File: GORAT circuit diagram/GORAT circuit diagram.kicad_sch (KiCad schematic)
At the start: 41 parts, among them J1 NMJ4HFD2, J2 NMJ4HFD2, J3 Barrel_Jack_PTH_Slot, U1 LM308N

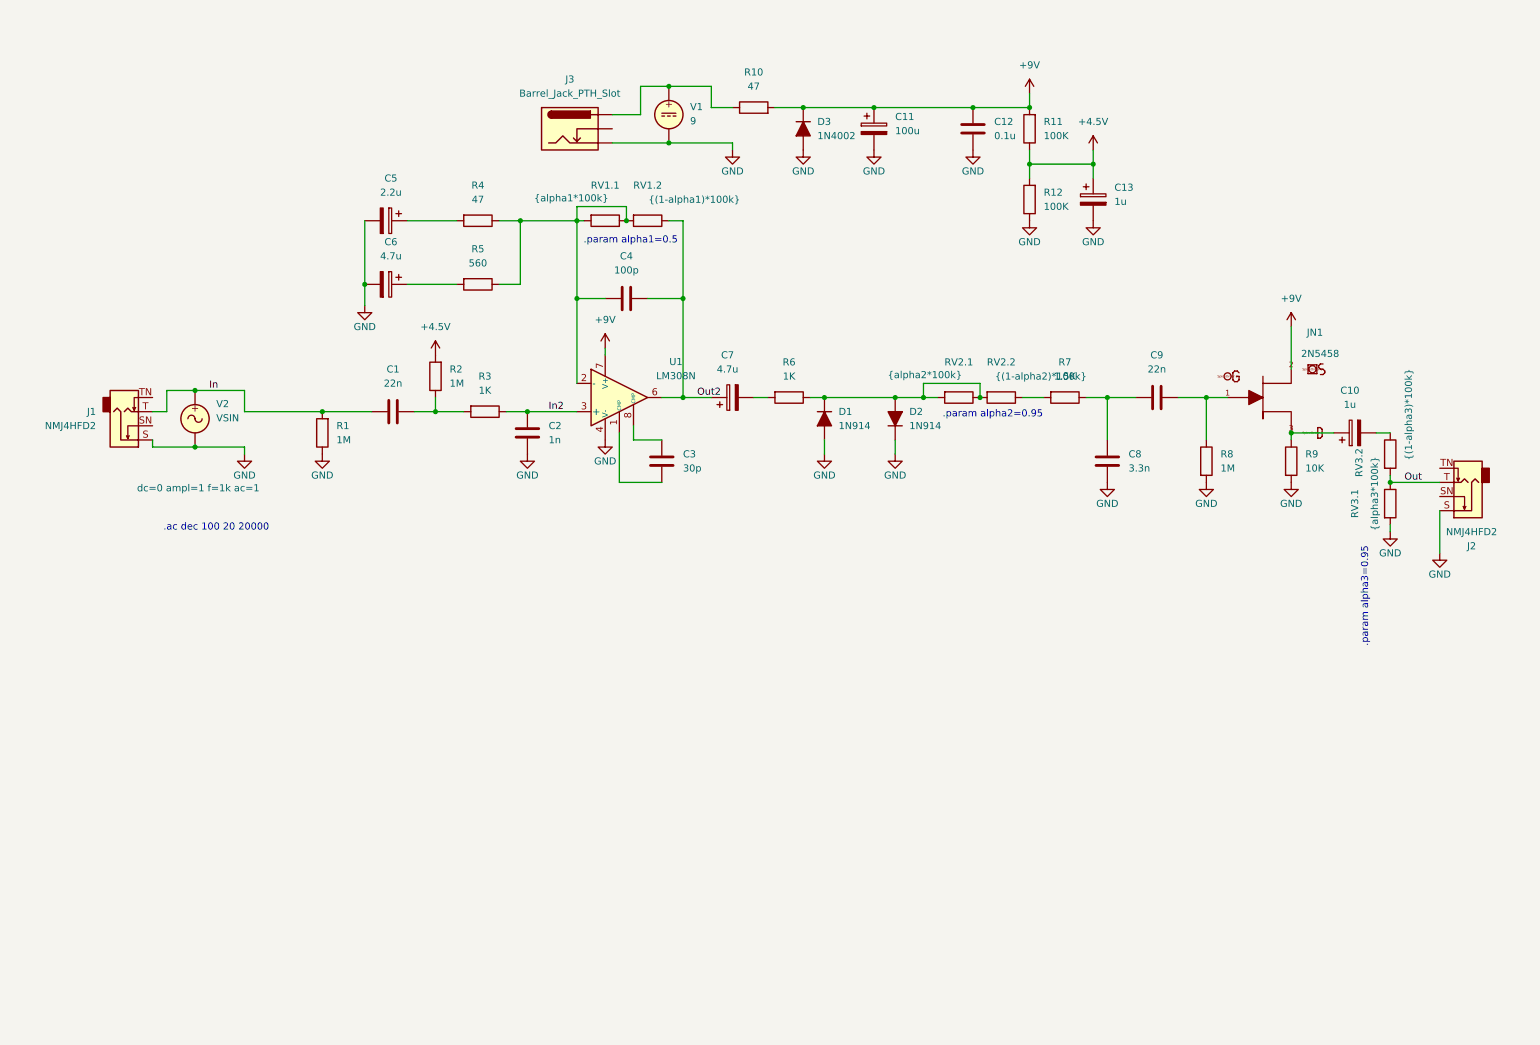
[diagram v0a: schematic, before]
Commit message: Update KiCad PCB and add backups
Replace GORAT circuit diagram.kicad_pcb with the full PCB data (expanded footprints, nets, layers and layout). Update related project files (GORAT circuit diagram.kicad_pro, .kicad_sch and fp-info-cache). Add multiple timestamped backup ZIPs under GORAT circuit diagram/GORAT circuit diagram-backups (dates 2026-02-27 and 2026-03-02).
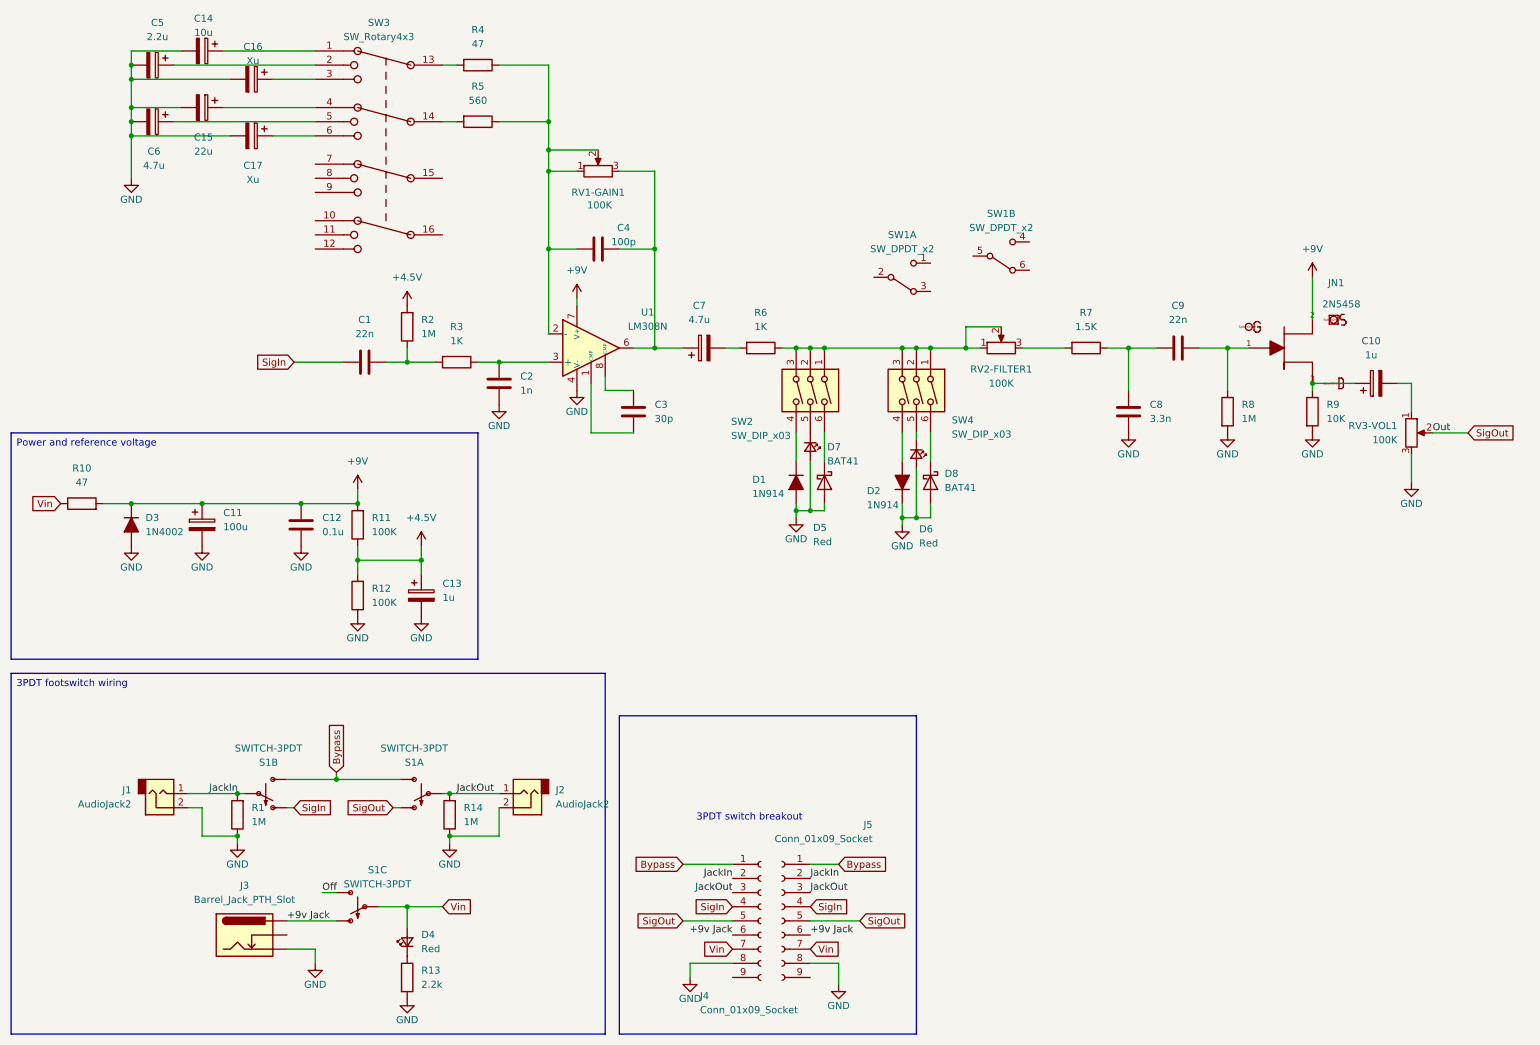
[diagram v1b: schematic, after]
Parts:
- removed J1, J2: NMJ4HFD2, Connector_Audio:Jack_6.35mm_Neutrik_NMJ4HFD2_Horizontal, symbol Connector_Audio:NMJ4HFD2
- removed RV1.1: {alpha1*100k}, symbol Device:R
- removed RV1.2: {(1-alpha1)*100k}, symbol Device:R
- removed RV2.1: {alpha2*100k}, symbol Device:R
- removed RV2.2: {(1-alpha2)*100k}, symbol Device:R
- removed RV3.1: {alpha3*100k}, symbol Device:R
- removed RV3.2: {(1-alpha3)*100k}, symbol Device:R
- removed V1: 9, symbol Simulation_SPICE:VDC
- removed V2: VSIN, symbol Simulation_SPICE:VSIN
- added C14: 10u, Capacitor_THT:CP_Radial_D5.0mm_P2.50mm, symbol Device:C_Polarized
- added C15: 22u, Capacitor_THT:CP_Radial_D5.0mm_P2.50mm, symbol Device:C_Polarized
- added C16, C17: Xu, Capacitor_THT:CP_Radial_D5.0mm_P2.50mm, symbol Device:C_Polarized
- added D4, D5, D6: Red, PCM_SparkFun-LED:LED_5mm_PTH_Red_NoSilk, symbol PCM_SparkFun-LED:LED_Red_5mm_PTH_NoSilk
- added D7, D8: BAT41, Diode_THT:D_DO-35_SOD27_P7.62mm_Horizontal, symbol Diode:BAT41
- added J1, J2: AudioJack2, Connector_Wire:SolderWire-0.75sqmm_1x02_P7mm_D1.25mm_OD3.5mm, symbol Connector_Audio:AudioJack2
- added J4, J5: Conn_01x09_Socket, Connector_PinHeader_2.54mm:PinHeader_1x09_P2.54mm_Vertical, symbol Connector:Conn_01x09_Socket
- added R13: 2.2k, Resistor_THT:R_Axial_DIN0207_L6.3mm_D2.5mm_P10.16mm_Horizontal, symbol Device:R
- added R14: 1M, Resistor_THT:R_Axial_DIN0207_L6.3mm_D2.5mm_P10.16mm_Horizontal, symbol Device:R
- added RV1-GAIN1, RV2-FILTER1, RV3-VOL1: 100K, Connector_Wire:SolderWire-0.75sqmm_1x03_P7mm_D1.25mm_OD3.5mm, symbol Device:R_Potentiometer
- added S1: SWITCH-3PDT, Daves customs:3PDT, symbol SparkFun-Electromechanical:SWITCH-3PDT
- added SW1: SW_DPDT_x2, symbol KRS_Switch:SW_DPDT_x2
- added SW2, SW4: SW_DIP_x03, symbol Switch:SW_DIP_x03
- added SW3: SW_Rotary4x3, Daves customs:Rotary Switch, symbol KRS_Switch:SW_Rotary4x3
- C1, C12, C2, C3, C4, C8, C9: footprint (none) -> Capacitor_THT:C_Disc_D4.7mm_W2.5mm_P5.00mm
- C10, C11, C13, C5, C6, C7: footprint (none) -> Capacitor_THT:CP_Radial_D5.0mm_P2.50mm
- R1, R10, R11, R12, R2, R3, R4, R5, R6, R7, R8, R9: footprint (none) -> Resistor_THT:R_Axial_DIN0207_L6.3mm_D2.5mm_P10.16mm_Horizontal
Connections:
- net GND: now also C14.2, C15.2, C16.2, C17.2, D5.2 (A), D6.2 (A), D7.2 (A), D8.2 (A), J1.2, J2.2, J4.8 (Pin_8), J5.8 (Pin_8), R13.2, R14.1, RV3-VOL1.3
- net at C4.2, R4.1, R5.1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: now also RV1-GAIN1.1, RV1-GAIN1.2
- net at R5.2: now also SW3.14; no longer C6.1
- net at C10.2: now also RV3-VOL1.1
- net +9v Jack: now reaches J3.PWR
- net +9v Jack: now also J4.6 (Pin_6), J5.6 (Pin_6), S1.P$7 (O); no longer R10.1
- net at R4.2: now also SW3.13; no longer C5.1
- net at R7.2: now also RV2-FILTER1.3
- net In renamed JackIn
- net JackIn: now also J1.1, J4.2 (Pin_2), J5.2 (Pin_2), S1.P$5 (P); no longer C1.1
- net In2: no longer names the net of C2.2, R3.1, U1.3 (+)
- net Out2: no longer names the net of C4.1, C7.1, U1.6
- net Out2: now also RV1-GAIN1.3
- new net: D4.1 (K), R13.1
- new net: D8.1 (K), SW4.6
- new net: D2.2 (A), SW4.4
- new net: R6.1, RV2-FILTER1.1, RV2-FILTER1.2, SW2.1, SW2.2, SW2.3, SW4.1, SW4.2, SW4.3
- new net: C17.1, SW3.6
- new net: D1.1 (K), SW2.4
- new net: C15.1, SW3.4
- new net: D7.1 (K), SW2.6
- new net: D5.1 (K), SW2.5
- new net: C14.1, SW3.1
- new net: C5.1, SW3.2
- new net: C16.1, SW3.3
- new net: C6.1, SW3.5
- new net: D6.1 (K), SW4.5
- new net Bypass: J4.1 (Pin_1), J5.1 (Pin_1), S1.P$3 (S), S1.P$6 (S)
- new net JackOut: J2.1, J4.3 (Pin_3), J5.3 (Pin_3), R14.2, S1.P$2 (P)
- new net Off: S1.P$9 (S)
- new net SigIn: C1.1, J4.4 (Pin_4), J5.4 (Pin_4), S1.P$4 (O)
- new net SigOut: J4.5 (Pin_5), J5.5 (Pin_5), RV3-VOL1.2, S1.P$1 (O)
- new net Vin: D4.2 (A), J4.7 (Pin_7), J5.7 (Pin_7), R10.1, S1.P$8 (P)
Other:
- note added: "3PDT switch breakout"
- note removed: ".ac dec 100 20 20000"
- note removed: ".param alpha1=0.5"
- note removed: ".param alpha2=0.95"
- note removed: ".param alpha3=0.95"
- moved on the sheet: C1, C10, C11, C12, C13, C2, C3, C4, C5, C6, C7, C8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

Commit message: asdsa
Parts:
- removed SW1: SW_DPDT_x2, symbol KRS_Switch:SW_DPDT_x2
- added C18: 470n, Capacitor_THT:C_Disc_D4.7mm_W2.5mm_P5.00mm, symbol Device:C
- added C19: 1u, Capacitor_THT:CP_Radial_D5.0mm_P2.50mm, symbol Device:C_Polarized
- added R15, R16, R17: 22k, Resistor_THT:R_Axial_DIN0207_L6.3mm_D2.5mm_P10.16mm_Horizontal, symbol Device:R
- added R18: 1M, Resistor_THT:R_Axial_DIN0207_L6.3mm_D2.5mm_P10.16mm_Horizontal, symbol Device:R
- added RV4-BLEND1: 100K, Connector_Wire:SolderWire-0.75sqmm_1x06_P7mm_D1.25mm_OD3.5mm, symbol Device:R_Potentiometer_Dual_Separate
- added U2, U3: TL072ACP, PCM_Package_DIP_AKL:DIP-8_W7.62mm_LongPads, symbol PCM_Amplifier_Operational_AKL:TL072ACP
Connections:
- net +4.5V: now also R18.1
- net +9V: now also U2.8 (V+), U3.8 (V+)
- net GND: now also U2.4 (V-), U3.4 (V-)
- net SigOut: now also C19.2; no longer RV3-VOL1.2
- net at C1.2, R2.1: now also U2.3 (+); no longer R3.2
- new net: R17.1, RV4-BLEND1.6
- new net: R15.1, R16.2, R17.2, U3.2 (-)
- new net: C18.1, U2.5 (+), U2.7
- new net: R3.2, U2.1, U2.2 (-), U2.6 (-)
- new net: C19.1, R15.2, U3.1
- new net: R16.1, RV4-BLEND1.3
- new net: R18.2, U3.3 (+)
- new net SigDRY: C18.2, RV4-BLEND1.4, RV4-BLEND1.5
- new net SigRAT: RV3-VOL1.2, RV4-BLEND1.1, RV4-BLEND1.2
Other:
- moved on the sheet: C1, R2

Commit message: almost done
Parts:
- removed J3: Barrel_Jack_PTH_Slot, PCM_SparkFun-Connector:Barrel_Jack_PTH_Slot, symbol PCM_SparkFun-Connector:Barrel_Jack_PTH_Slot
- removed J4, J5: Conn_01x09_Socket, Connector_PinHeader_2.54mm:PinHeader_1x09_P2.54mm_Vertical, symbol Connector:Conn_01x09_Socket
- removed SW2, SW4: SW_DIP_x03, symbol Switch:SW_DIP_x03
- added J3, J4: Conn_01x08_Socket, Connector_PinHeader_2.54mm:PinHeader_1x08_P2.54mm_Vertical, symbol Connector:Conn_01x08_Socket
- added J5, J7: Conn_01x02_Socket, Connector_PinHeader_2.54mm:PinHeader_1x02_P2.54mm_Vertical, symbol Connector:Conn_01x02_Socket
- added J6: Barrel_Jack, Connector_Wire:SolderWire-0.5sqmm_1x02_P4.6mm_D0.9mm_OD2.1mm, symbol Connector:Barrel_Jack
- added J8, J9: Conn_01x03_Socket, Connector_PinHeader_2.54mm:PinHeader_1x03_P2.54mm_Vertical, symbol Connector:Conn_01x03_Socket
- added SW8: SW_Rotary2x6, Daves customs:RS26, symbol KRS_Switch:SW_Rotary2x6
- RV1-GAIN1, RV2-FILTER1, RV3-VOL1: footprint Connector_Wire:SolderWire-0.75sqmm_1x03_P7mm_D1.25mm_OD3.5mm -> Daves customs:Potentiometer_Alpha_RD901F-40-00D_Single_Vertical
- RV4-BLEND1: footprint Connector_Wire:SolderWire-0.75sqmm_1x06_P7mm_D1.25mm_OD3.5mm -> Potentiometer_THT:Potentiometer_Alpha_RD902F-40-00D_Dual_Vertical
- SW3: footprint Daves customs:Rotary Switch -> Daves customs:RS26
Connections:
- net GND: now also RV3-VOL1.1, J6.2, J7.2 (Pin_2), J9.3 (Pin_3); no longer C14.2, C15.2, C16.2, C17.2, C5.2, C6.2, D1.2 (A), D2.1 (K), D5.2 (A), D6.2 (A), D7.2 (A), D8.2 (A), RV3-VOL1.3
- net SigDRY: no longer RV4-BLEND1.5
- net SigIn: no longer S1.P$4 (O)
- net SigOut: no longer S1.P$1 (O)
- net at C4.2, RV1-GAIN1.1, RV1-GAIN1.2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: now also J7.1 (Pin_1); no longer R4.1, R5.1
- net GND3: now reaches D8.1 (K)
- net GND3: now also C14.2, C15.2, C16.2, C17.2, C5.2, C6.2, D1.2 (A), D2.1 (K), D5.2 (A), D6.1 (K), D7.2 (A), J5.2 (Pin_2), J8.3 (Pin_3)
- net at D2.2 (A): now also SW8.3, SW8.4
- net at C10.2: now also RV3-VOL1.3; no longer RV3-VOL1.1
- net at R17.1, RV4-BLEND1.6: now also RV4-BLEND1.5
- net at R6.1, RV2-FILTER1.1: now also J9.1 (Pin_1), J9.2 (Pin_2); no longer RV2-FILTER1.2
- net at D1.1 (K): now also SW8.11, SW8.9
- net at D7.1 (K): now also SW8.12, SW8.7
- net at D5.1 (K): now also SW8.8
- net at R7.2, RV2-FILTER1.3: now also RV2-FILTER1.2
- net +9v Jack renamed +9v Jack2
- net +9v Jack2: now also J4.6 (Pin_6)
- net Bypass: no longer names the net of S1.P$3 (S), S1.P$6 (S)
- net JackIn renamed JackIn1
- net JackIn1: now also J3.2 (Pin_2); no longer S1.P$5 (P)
- net JackOut renamed JackOut1
- net JackOut1: now also J3.3 (Pin_3); no longer S1.P$2 (P)
- net Vin renamed Vin1
- net Vin1: now also J3.7 (Pin_7); no longer S1.P$8 (P)
- new net: D8.2 (A), SW8.1, SW8.5
- new net: J5.1 (Pin_1), R4.1, R5.1
- new net: J8.1 (Pin_1), SW8.13
- new net: J8.2 (Pin_2), SW8.14
- new net: D6.2 (A), SW8.2, SW8.6
- new net +9v Jack1: J3.6 (Pin_6), J6.1
- new net Bypass1: J3.1 (Pin_1)
- new net Bypass2: J4.1 (Pin_1)
- new net GND1: J3.8 (Pin_8)
- new net GND2: J4.8 (Pin_8)
- new net JackIn2: J4.2 (Pin_2), S1.P$5 (P)
- new net JackOut2: J4.3 (Pin_3), S1.P$2 (P)
- new net SigIn1: J3.4 (Pin_4)
- new net SigIn2: J4.4 (Pin_4), S1.P$4 (O)
- new net SigOut1: J3.5 (Pin_5)
- new net SigOut2: J4.5 (Pin_5), S1.P$1 (O)
- new net Vin2: J4.7 (Pin_7), S1.P$8 (P)
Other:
- moved on the sheet: C14, C15, C16, C17, C5, C6, D1, D2, D4, D5, D7, D8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

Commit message: close to done
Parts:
- removed C16, C17: Xu, Capacitor_THT:CP_Radial_D5.0mm_P2.50mm, symbol Device:C_Polarized
- removed C3: 30p, Capacitor_THT:C_Disc_D4.7mm_W2.5mm_P5.00mm, symbol Device:C
- removed JN1: 2N5458, 2N5458:TO92, symbol 2N5458:2N5458
- added C16: 68p, Capacitor_THT:C_Disc_D4.7mm_W2.5mm_P5.00mm, symbol Device:C
- added C17: 47p, Capacitor_THT:C_Disc_D4.7mm_W2.5mm_P5.00mm, symbol Device:C
- added C20: 220n, Capacitor_THT:C_Disc_D5.1mm_W3.2mm_P5.00mm, symbol Device:C
- added C21: 470n, Capacitor_THT:C_Disc_D5.1mm_W3.2mm_P5.00mm, symbol Device:C
- added C22: 33p, Capacitor_THT:C_Disc_D4.7mm_W2.5mm_P5.00mm, symbol Device:C
- added J10, J11: Conn_01x02_Socket, Connector_PinHeader_2.54mm:PinHeader_1x02_P2.54mm_Vertical, symbol Connector:Conn_01x02_Socket
- added Q1: J111, PCM_Package_TO_SOT_THT_AKL:TO-92_Inline_Wide_DSG, symbol PCM_Transistor_JFET_AKL:J111
- U1: value LM308N -> OP07CP
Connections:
- net +9V: now also Q1.1 (D)
- net GND3: now also C20.1, C21.1
- net at C9.1, R8.1: now also Q1.3 (G)
- net at C10.1, R9.1: now also Q1.2 (S)
- net at SW3.6: now also C21.2
- net at U1.1 (CMP): now also J10.2 (Pin_2)
- net at U1.8 (CMP): now also J10.1 (Pin_1)
- net at SW3.15: now also J11.1 (Pin_1)
- net at SW3.3: now also C20.2
- net at SW3.7: now also C16.1
- net at SW3.8: now also C17.1
- net at SW3.9: now also C22.1
- new net: C16.2, C17.2, C22.2, J11.2 (Pin_2)
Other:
- note added: "Bass, Reg, Beans"
- moved on the sheet: C14, C15, C5, C6, J5, J7
